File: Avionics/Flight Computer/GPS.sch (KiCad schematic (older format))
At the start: 6 parts, among them J6 734120110, U9 MAX-M8W

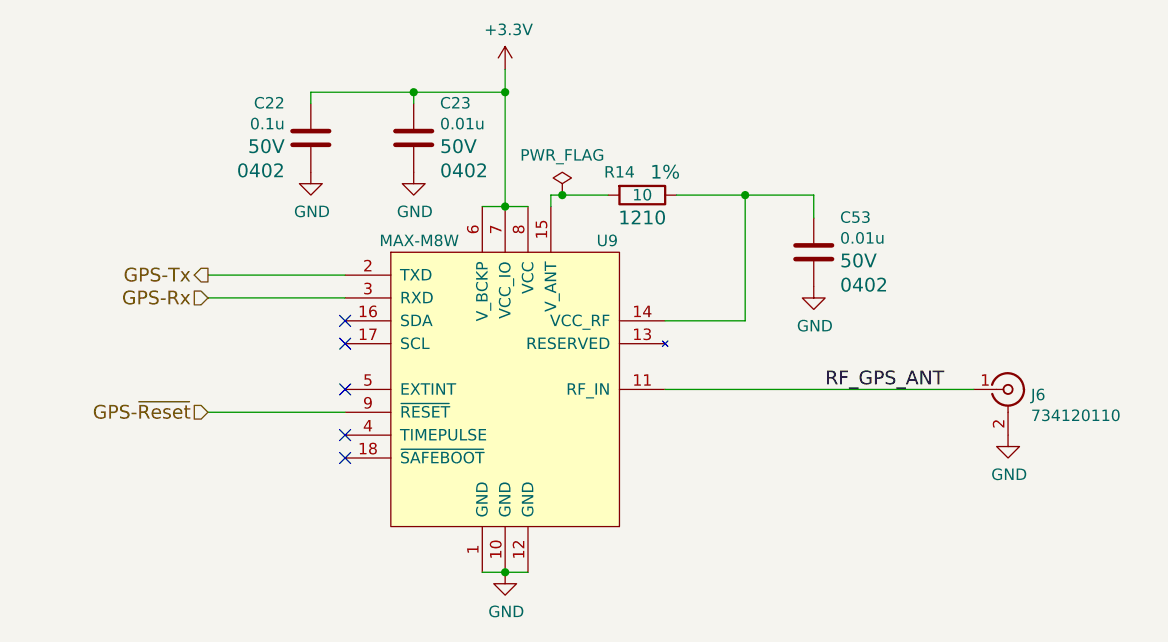
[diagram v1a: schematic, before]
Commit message: Changed LED configuration, added smart driver chip to let all the CPUs access it..
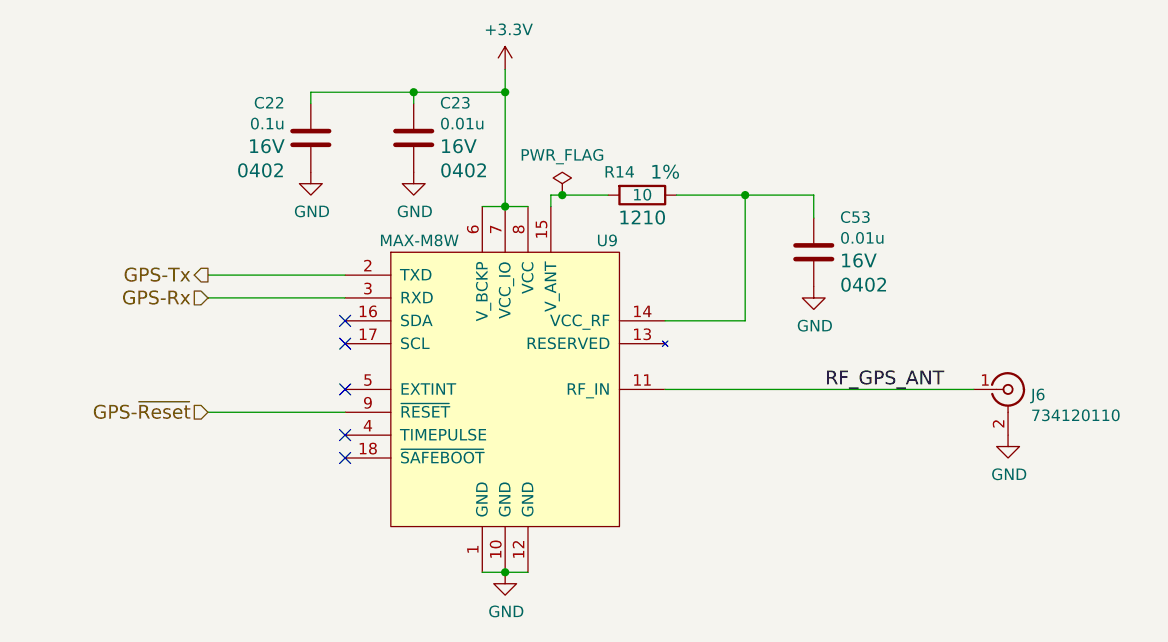
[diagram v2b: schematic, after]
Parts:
- C22, C23, C53, R14: Voltage 50V -> 16V
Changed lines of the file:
@@
 $EndComp
 $Comp
-L GND #PWR0112
+L GND #PWR0116
 U 1 1 58AF392E
 P 6750 3650
-F 0 "#PWR0112" H 6800 3700 50  0001 C CNN
+F 0 "#PWR0116" H 6800 3700 50  0001 C CNN
 F 1 "GND" H 6755 3477 50  0000 C CNN
 F 2 "" H -50 -100 50  0001 C CNN
@@
 F 3 "" V -1320 -100 50  0001 C CNN
 F 4 "1%" V 5050 2700 60  0000 C CNN "Tolerance"
-F 5 "50V" V -1150 -100 60  0001 C CNN "Voltage"
+F 5 "16V" V -1150 -100 60  0001 C CNN "Voltage"
 F 6 "0.5W" V -1050 -100 60  0001 C CNN "Power"
 F 7 "Thin Film" V -950 -100 60  0001 C CNN "Material"
@@
 F 2 "Capacitors_SMD:C_0402" H 188 0   50  0001 C CNN
 F 3 "" H 150 150 50  0001 C CNN
-F 4 "50V" H 6015 2812 60  0000 L CNN "Voltage"
+F 4 "16V" H 6015 2812 60  0000 L CNN "Voltage"
 F 5 "20%" H 6015 2759 60  0001 L CNN "Tolerance"
 F 6 "X7R" H 6015 2706 60  0001 L CNN "Type"
@@
 $EndComp
 $Comp
-L GND #PWR0113
+L GND #PWR0117
 U 1 1 58B48996
 P 5900 3000
-F 0 "#PWR0113" H 5950 3050 50  0001 C CNN
+F 0 "#PWR0117" H 5950 3050 50  0001 C CNN
 F 1 "GND" H 5905 2827 50  0000 C CNN
 F 2 "" H -900 -750 50  0001 C CNN
@@
 	4550 2050 4550 2650
 $Comp
-L +3.3V #PWR0114
+L +3.3V #PWR0118
 U 1 1 58B4A068
 P 4550 2050
-F 0 "#PWR0114" H 0   -500 50  0001 C CNN
+F 0 "#PWR0118" H 0   -500 50  0001 C CNN
 F 1 "+3.3V" H 4565 2223 50  0000 C CNN
 F 2 "" H 0   -350 50  0001 C CNN
@@
 F 2 "Capacitors_SMD:C_0402" H -1562 -500 50  0001 C CNN
 F 3 "" H -1600 -350 50  0001 C CNN
-F 4 "50V" H 4265 2312 60  0000 L CNN "Voltage"
+F 4 "16V" H 4265 2312 60  0000 L CNN "Voltage"
 F 5 "20%" H 4265 2259 60  0001 L CNN "Tolerance"
 F 6 "X7R" H 4265 2206 60  0001 L CNN "Type"
@@
 Connection ~ 4550 2150
 $Comp
-L GND #PWR0115
+L GND #PWR0119
 U 1 1 58B4A18F
 P 4150 2500
-F 0 "#PWR0115" H 4200 2550 50  0001 C CNN
+F 0 "#PWR0119" H 4200 2550 50  0001 C CNN
 F 1 "GND" H 4155 2327 50  0000 C CNN
 F 2 "" H -2650 -1250 50  0001 C CNN
@@
 F 2 "Capacitors_SMD:C_0402" H -2012 -500 50  0001 C CNN
 F 3 "" H -2050 -350 50  0001 C CNN
-F 4 "50V" H 3586 2312 60  0000 R CNN "Voltage"
+F 4 "16V" H 3586 2312 60  0000 R CNN "Voltage"
 F 5 "20%" H 3815 2259 60  0001 L CNN "Tolerance"
 F 6 "X7R" H 3815 2206 60  0001 L CNN "Type"
@@
 $EndComp
 $Comp
-L GND #PWR0116
+L GND #PWR0120
 U 1 1 58B4A1E4
 P 3700 2500
-F 0 "#PWR0116" H 3750 2550 50  0001 C CNN
+F 0 "#PWR0120" H 3750 2550 50  0001 C CNN
 F 1 "GND" H 3705 2327 50  0000 C CNN
 F 2 "" H -3100 -1250 50  0001 C CNN
@@
 NoConn ~ 3850 3750
 $Comp
-L GND #PWR0117
+L GND #PWR0121
 U 1 1 58B4A393
 P 4550 4250
-F 0 "#PWR0117" H 4600 4300 50  0001 C CNN
+F 0 "#PWR0121" H 4600 4300 50  0001 C CNN
 F 1 "GND" H 4555 4077 50  0000 C CNN
 F 2 "" H -2250 500 50  0001 C CNN
@@
 NoConn ~ 3850 3650
 $Comp
-L PWR_FLAG #FLG0118
+L PWR_FLAG #FLG0122
 U 1 1 58BF1BFF
 P 4800 2600
-F 0 "#FLG0118" H -450 525 50  0001 C CNN
+F 0 "#FLG0122" H -450 525 50  0001 C CNN
 F 1 "PWR_FLAG" H 4800 2774 50  0000 C CNN
 F 2 "" H -450 450 50  0001 C CNN

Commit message: Added Logo, connected GPS SDA/SCL, and cleaned silk.
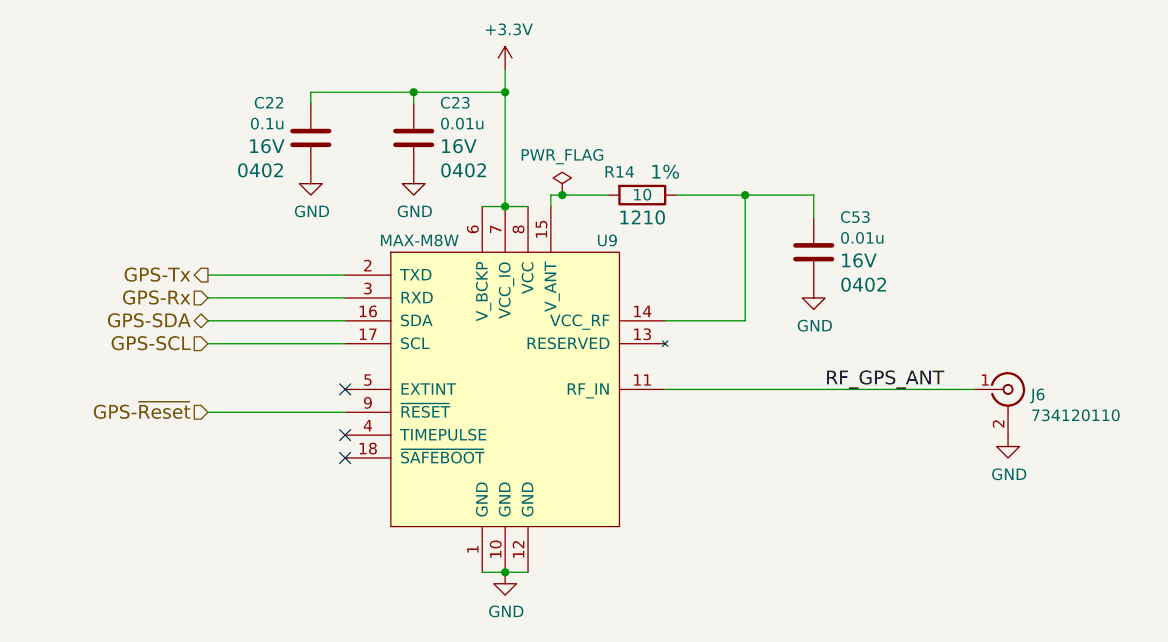
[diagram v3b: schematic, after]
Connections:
- net GPS-SDA: now reaches U9.16 (SDA)
- net GPS-SCL: now reaches U9.17 (SCL)
- no-connect marks 5 -> 3
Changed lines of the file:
@@
 RF_GPS_ANT
-$Comp
-L MAX-M8W U9
-U 1 1 58AFAC85
-P 4550 3450
-F 0 "U9" H 4950 4100 50  0000 L CNN
-F 1 "MAX-M8W" H 4000 4100 50  0000 L CNN
-F 2 "RF_Modules:U-BLOX-MAX" H 400 -200 50  0001 C CNN
-F 3 "https://www.u-blox.com/sites/default/files/MAX-M8-FW3_DataSheet_%28UBX-15031506%29.pdf" H -300 -1350 50  0001 C CNN
-	1    4550 3450
-	1    0    0    -1
-$EndComp
 $Comp
 L R R14
@@
 	3700 2200 3700 2150
 Connection ~ 4150 2150
-NoConn ~ 3850 3250
-NoConn ~ 3850 3150
 NoConn ~ 3850 3750
 $Comp
@@
 $EndComp
 Connection ~ 4800 2600
+Text HLabel 3250 3250 0    60   Input ~ 0
+GPS-SCL
+Text HLabel 3250 3150 0    60   BiDi ~ 0
+GPS-SDA
+$Comp
+L MAX-M8W U9
+U 1 1 58AFAC85
+P 4550 3450
+F 0 "U9" H 4950 4100 50  0000 L CNN
+F 1 "MAX-M8W" H 4000 4100 50  0000 L CNN
+F 2 "RF_Modules:U-BLOX-MAX" H 400 -200 50  0001 C CNN
+F 3 "https://www.u-blox.com/sites/default/files/MAX-M8-FW3_DataSheet_%28UBX-15031506%29.pdf" H -300 -1350 50  0001 C CNN
+	1    4550 3450
+	1    0    0    -1
+$EndComp
+Wire Wire Line
+	3250 3150 3850 3150
+Wire Wire Line
+	3850 3250 3250 3250
 $EndSCHEMATC

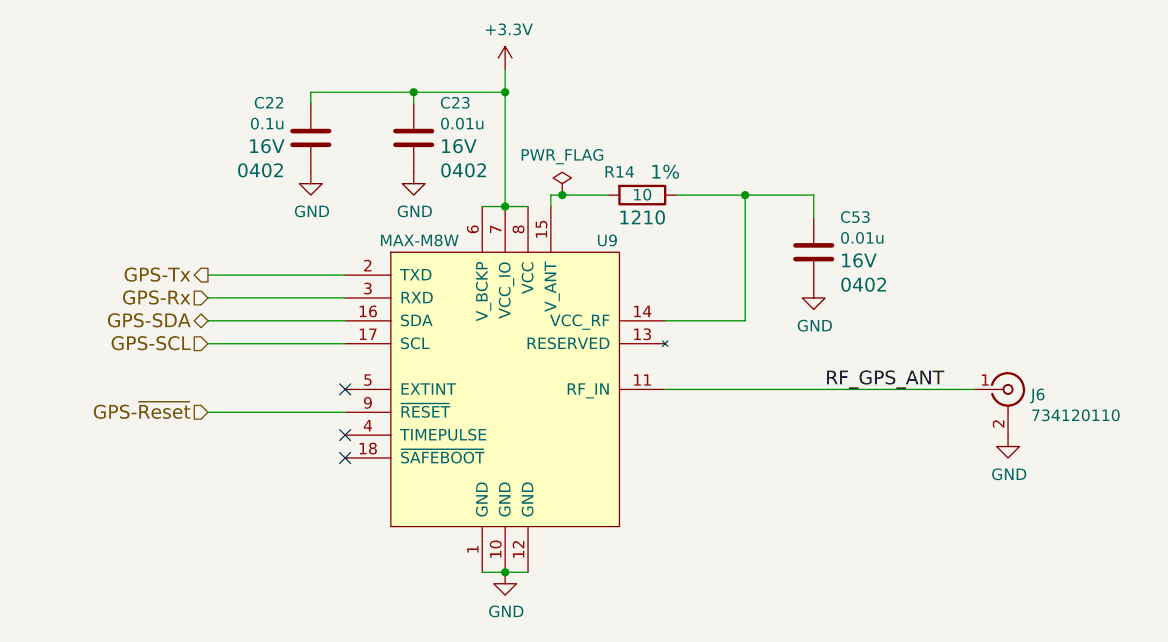
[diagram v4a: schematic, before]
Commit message: Built outputs and added manufacturing part numbers to make BOM search easier.
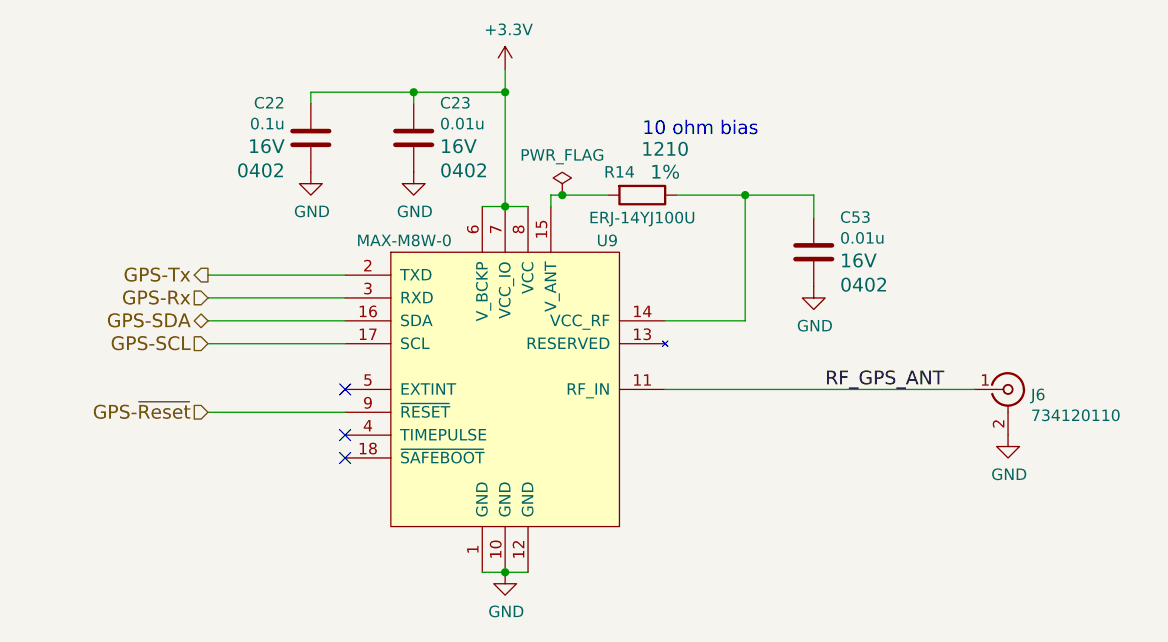
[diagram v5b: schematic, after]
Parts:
- R14: value 10 -> ERJ-14YJ100U
- U9: value MAX-M8W -> MAX-M8W-0
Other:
- note added: "10 ohm bias"
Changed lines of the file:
@@
 $EndComp
 $Comp
-L GND #PWR108
+L GND #PWR0116
 U 1 1 58AF392E
 P 6750 3650
-F 0 "#PWR108" H 6800 3700 50  0001 C CNN
+F 0 "#PWR0116" H 6800 3700 50  0001 C CNN
 F 1 "GND" H 6755 3477 50  0000 C CNN
 F 2 "" H -50 -100 50  0001 C CNN
@@
 P 5150 2600
 F 0 "R14" V 5050 2500 50  0000 C CNN
-F 1 "10" V 5150 2600 50  0000 C CNN
+F 1 "ERJ-14YJ100U" V 5250 2600 50  0000 C CNN
 F 2 "Resistors_SMD:R_1210" V -1600 -100 50  0001 C CNN
 F 3 "" V -1320 -100 50  0001 C CNN
@@
 F 6 "0.5W" V -1050 -100 60  0001 C CNN "Power"
 F 7 "Thin Film" V -950 -100 60  0001 C CNN "Material"
-F 8 "1210" V 5250 2600 60  0000 C CNN "Package"
+F 8 "1210" V 4950 2700 60  0000 C CNN "Package"
 	1    5150 2600
 	0    1    1    0
@@
 $EndComp
 $Comp
-L GND #PWR107
+L GND #PWR0117
 U 1 1 58B48996
 P 5900 3000
-F 0 "#PWR107" H 5950 3050 50  0001 C CNN
+F 0 "#PWR0117" H 5950 3050 50  0001 C CNN
 F 1 "GND" H 5905 2827 50  0000 C CNN
 F 2 "" H -900 -750 50  0001 C CNN
@@
 	4550 2050 4550 2650
 $Comp
-L +3.3V #PWR105
+L +3.3V #PWR0118
 U 1 1 58B4A068
 P 4550 2050
-F 0 "#PWR105" H 0   -500 50  0001 C CNN
+F 0 "#PWR0118" H 0   -500 50  0001 C CNN
 F 1 "+3.3V" H 4565 2223 50  0000 C CNN
 F 2 "" H 0   -350 50  0001 C CNN
@@
 Connection ~ 4550 2150
 $Comp
-L GND #PWR104
+L GND #PWR0119
 U 1 1 58B4A18F
 P 4150 2500
-F 0 "#PWR104" H 4200 2550 50  0001 C CNN
+F 0 "#PWR0119" H 4200 2550 50  0001 C CNN
 F 1 "GND" H 4155 2327 50  0000 C CNN
 F 2 "" H -2650 -1250 50  0001 C CNN
@@
 $EndComp
 $Comp
-L GND #PWR103
+L GND #PWR0120
 U 1 1 58B4A1E4
 P 3700 2500
-F 0 "#PWR103" H 3750 2550 50  0001 C CNN
+F 0 "#PWR0120" H 3750 2550 50  0001 C CNN
 F 1 "GND" H 3705 2327 50  0000 C CNN
 F 2 "" H -3100 -1250 50  0001 C CNN
@@
 NoConn ~ 3850 3750
 $Comp
-L GND #PWR106
+L GND #PWR0121
 U 1 1 58B4A393
 P 4550 4250
-F 0 "#PWR106" H 4600 4300 50  0001 C CNN
+F 0 "#PWR0121" H 4600 4300 50  0001 C CNN
 F 1 "GND" H 4555 4077 50  0000 C CNN
 F 2 "" H -2250 500 50  0001 C CNN
@@
 NoConn ~ 3850 3650
 $Comp
-L PWR_FLAG #FLG14
+L PWR_FLAG #FLG0122
 U 1 1 58BF1BFF
 P 4800 2600
-F 0 "#FLG14" H -450 525 50  0001 C CNN
+F 0 "#FLG0122" H -450 525 50  0001 C CNN
 F 1 "PWR_FLAG" H 4800 2774 50  0000 C CNN
 F 2 "" H -450 450 50  0001 C CNN
@@
 P 4550 3450
 F 0 "U9" H 4950 4100 50  0000 L CNN
-F 1 "MAX-M8W" H 4000 4100 50  0000 L CNN
+F 1 "MAX-M8W-0" H 3900 4100 50  0000 L CNN
 F 2 "RF_Modules:U-BLOX-MAX" H 400 -200 50  0001 C CNN
 F 3 "https://www.u-blox.com/sites/default/files/MAX-M8-FW3_DataSheet_%28UBX-15031506%29.pdf" H -300 -1350 50  0001 C CNN
@@
 Wire Wire Line
 	3850 3250 3250 3250
+Text Notes 5150 2350 0    60   ~ 0
+10 ohm bias
 $EndSCHEMATC

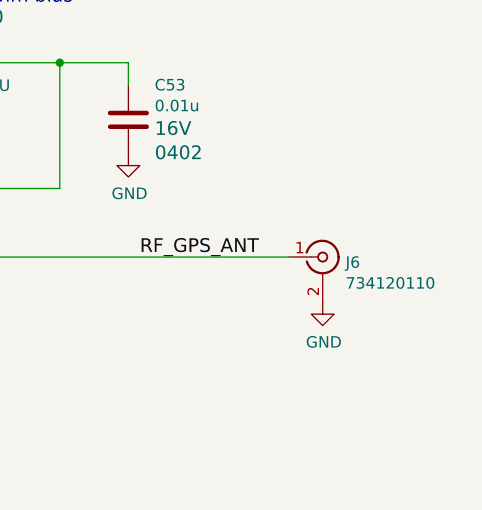
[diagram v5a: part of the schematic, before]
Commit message: Updated more manufacturing part numbers for macrofab compatibility.
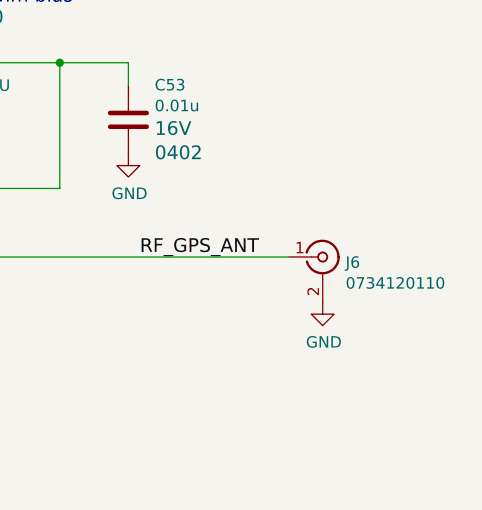
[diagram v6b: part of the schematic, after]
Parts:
- J6: value 734120110 -> 0734120110
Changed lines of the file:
@@
 P 6750 3450
 F 0 "J6" H 6850 3426 50  0000 L CNN
-F 1 "734120110" H 6850 3335 50  0000 L CNN
+F 1 "0734120110" H 6850 3335 50  0000 L CNN
 F 2 "Connectors_Molex:Molex_Microcoaxial_RF" H -350 750 50  0001 C CNN
 F 3 "http://www.molex.com/pdm_docs/sd/734120110_sd.pdf" H -350 750 50  0001 C CNN
